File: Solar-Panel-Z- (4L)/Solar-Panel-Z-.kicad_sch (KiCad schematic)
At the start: 82 parts, among them J1 FTS-105-01-L-DV-A, J2 U.FL-R-SMT-1, Q1 BSS138DWQ-7, Q2 MBT2222ADW1T1, Q3 BSS138DWQ-7, Q4 MBT2222ADW1T1, Q5 IRLML2803, U1 BQ25570RGRR, U2 TSL2561, U3 ATB2012-50011-T000, U4 NDS8434

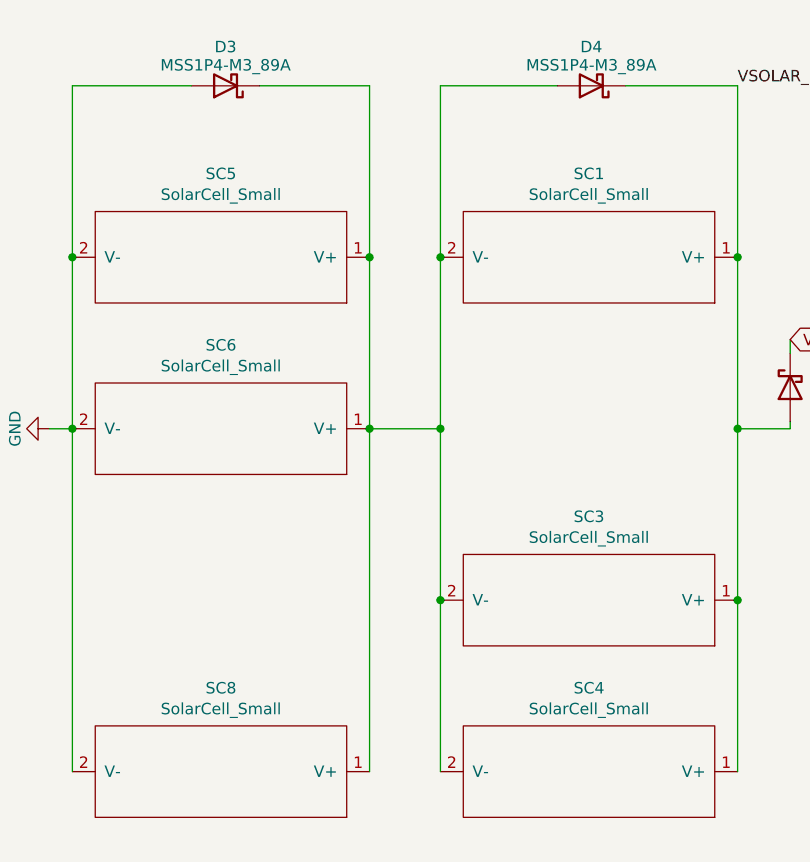
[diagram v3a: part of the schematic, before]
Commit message: Z- board antenna updates
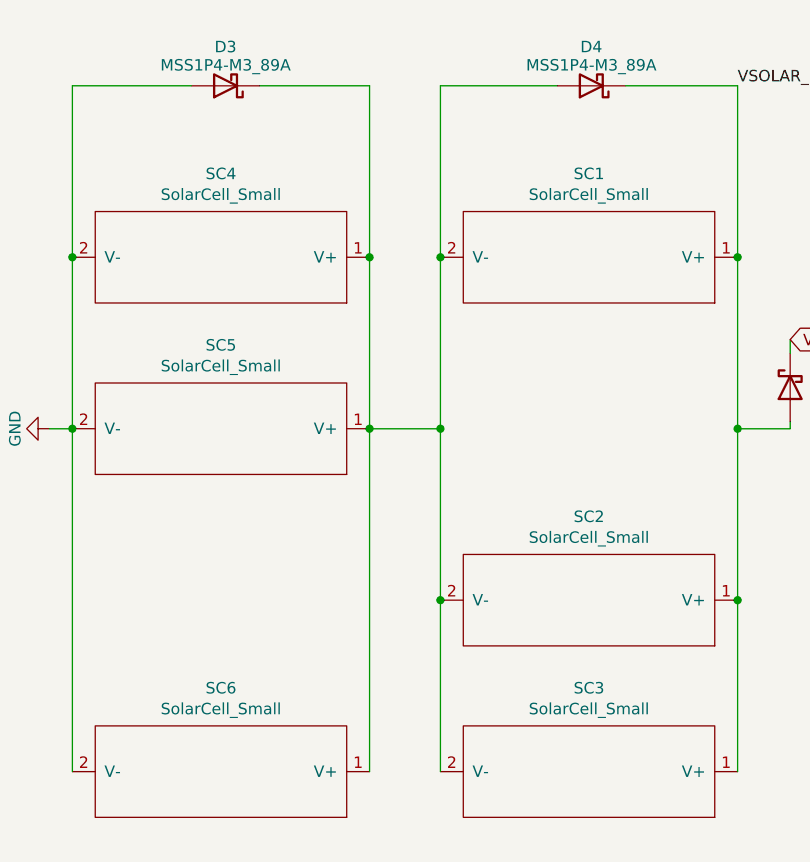
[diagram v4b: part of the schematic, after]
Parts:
- H5, H6: footprint solarpanels:Antenna Pad -> solarpanels:Antenna Mount
- renumbered SC3 to SC2, SC4 to SC3, SC5 to SC4, SC6 to SC5, SC8 to SC6
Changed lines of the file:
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@@
   (symbol (lib_name "SolarCell_Small_2") (lib_id "solarpanels:SolarCell_Small") (at 302.006 91.694 0) (mirror y) (unit 1)
     (in_bom yes) (on_board yes)
-    (property "Reference" "SC3" (id 0) (at 302.006 82.423 0))
+    (property "Reference" "SC2" (id 0) (at 302.006 82.423 0))
     (property "Value" "SolarCell_Small" (id 1) (at 302.006 84.7344 0))
     (property "Footprint" "solarpanels:KXOB25-05X3F" (id 2) (at 302.006 85.344 0)
@@
   (symbol (lib_name "SolarCell_Small_7") (lib_id "solarpanels:SolarCell_Small") (at 302.006 110.744 0) (mirror y) (unit 1)
     (in_bom yes) (on_board yes)
-    (property "Reference" "SC4" (id 0) (at 302.006 101.473 0))
+    (property "Reference" "SC3" (id 0) (at 302.006 101.473 0))
     (property "Value" "SolarCell_Small" (id 1) (at 302.006 103.7844 0))
     (property "Footprint" "solarpanels:KXOB25-05X3F" (id 2) (at 302.006 104.394 0)
@@
   (symbol (lib_name "SolarCell_Small_1") (lib_id "solarpanels:SolarCell_Small") (at 261.112 53.594 0) (mirror y) (unit 1)
     (in_bom yes) (on_board yes)
-    (property "Reference" "SC5" (id 0) (at 261.112 44.323 0))
+    (property "Reference" "SC4" (id 0) (at 261.112 44.323 0))
     (property "Value" "SolarCell_Small" (id 1) (at 261.112 46.6344 0))
     (property "Footprint" "solarpanels:KXOB25-05X3F" (id 2) (at 261.112 47.244 0)
@@
   (symbol (lib_name "SolarCell_Small_6") (lib_id "solarpanels:SolarCell_Small") (at 261.112 72.644 0) (mirror y) (unit 1)
     (in_bom yes) (on_board yes)
-    (property "Reference" "SC6" (id 0) (at 261.112 63.373 0))
+    (property "Reference" "SC5" (id 0) (at 261.112 63.373 0))
     (property "Value" "SolarCell_Small" (id 1) (at 261.112 65.6844 0))
     (property "Footprint" "solarpanels:KXOB25-05X3F" (id 2) (at 261.112 66.294 0)
@@
   (symbol (lib_id "solarpanels:SolarCell_Small") (at 261.112 110.744 0) (mirror y) (unit 1)
     (in_bom yes) (on_board yes)
-    (property "Reference" "SC8" (id 0) (at 261.112 101.473 0))
+    (property "Reference" "SC6" (id 0) (at 261.112 101.473 0))
     (property "Value" "SolarCell_Small" (id 1) (at 261.112 103.7844 0))
     (property "Footprint" "solarpanels:KXOB25-05X3F" (id 2) (at 261.112 104.394 0)
@@
       (effects (font (size 1.27 1.27)) (justify left) hide)
     )
-    (property "Footprint" "solarpanels:Antenna Pad" (id 2) (at 413.639 168.275 0)
+    (property "Footprint" "solarpanels:Antenna Mount" (id 2) (at 413.639 168.275 0)
       (effects (font (size 1.27 1.27)) hide)
     )
@@
       (effects (font (size 1.27 1.27)) (justify left) hide)
     )
-    (property "Footprint" "solarpanels:Antenna Pad" (id 2) (at 413.639 178.435 0)
+    (property "Footprint" "solarpanels:Antenna Mount" (id 2) (at 413.639 178.435 0)
       (effects (font (size 1.27 1.27)) hide)
     )
@@
     )
     (path "/149c927f-e288-46dd-abdb-0b1b1794eb2c"
-      (reference "H5") (unit 1) (value "MountingHole_Pad") (footprint "solarpanels:Antenna Pad")
+      (reference "H5") (unit 1) (value "MountingHole_Pad") (footprint "solarpanels:Antenna Mount")
     )
     (path "/8fe9a4c0-ef6b-4ec2-9e38-751b9e6e9ad9"
-      (reference "H6") (unit 1) (value "MountingHole_Pad") (footprint "solarpanels:Antenna Pad")
+      (reference "H6") (unit 1) (value "MountingHole_Pad") (footprint "solarpanels:Antenna Mount")
     )
     (path "/baaf2eaf-2642-4b8c-8f92-784b52992403"
@@
     )
     (path "/00000000-0000-0000-0000-00005db20459"
+      (reference "SC2") (unit 1) (value "SolarCell_Small") (footprint "solarpanels:KXOB25-05X3F")
+    )
+    (path "/00000000-0000-0000-0000-00005db20680"
       (reference "SC3") (unit 1) (value "SolarCell_Small") (footprint "solarpanels:KXOB25-05X3F")
     )
-    (path "/00000000-0000-0000-0000-00005db20680"
+    (path "/00000000-0000-0000-0000-00005db208db"
       (reference "SC4") (unit 1) (value "SolarCell_Small") (footprint "solarpanels:KXOB25-05X3F")
     )
-    (path "/00000000-0000-0000-0000-00005db208db"
+    (path "/00000000-0000-0000-0000-00005db20d87"
       (reference "SC5") (unit 1) (value "SolarCell_Small") (footprint "solarpanels:KXOB25-05X3F")
     )
-    (path "/00000000-0000-0000-0000-00005db20d87"
+    (path "/00000000-0000-0000-0000-00005db2144e"
       (reference "SC6") (unit 1) (value "SolarCell_Small") (footprint "solarpanels:KXOB25-05X3F")
     )
-    (path "/00000000-0000-0000-0000-00005db2144e"
-      (reference "SC8") (unit 1) (value "SolarCell_Small") (footprint "solarpanels:KXOB25-05X3F")
-    )
     (path "/00000000-0000-0000-0000-00005df513ae"
